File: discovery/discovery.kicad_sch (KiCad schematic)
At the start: 19 parts, among them J1 USB_C_Receptacle_USB2.0_16P, SW1 SW_Push, U1 RP2350_60QFN, U2 USBLC6-2SC6, U3 AP2114H-3.3TRG1, U4 W25Q32JVZP, X1 ABM8-272-T3

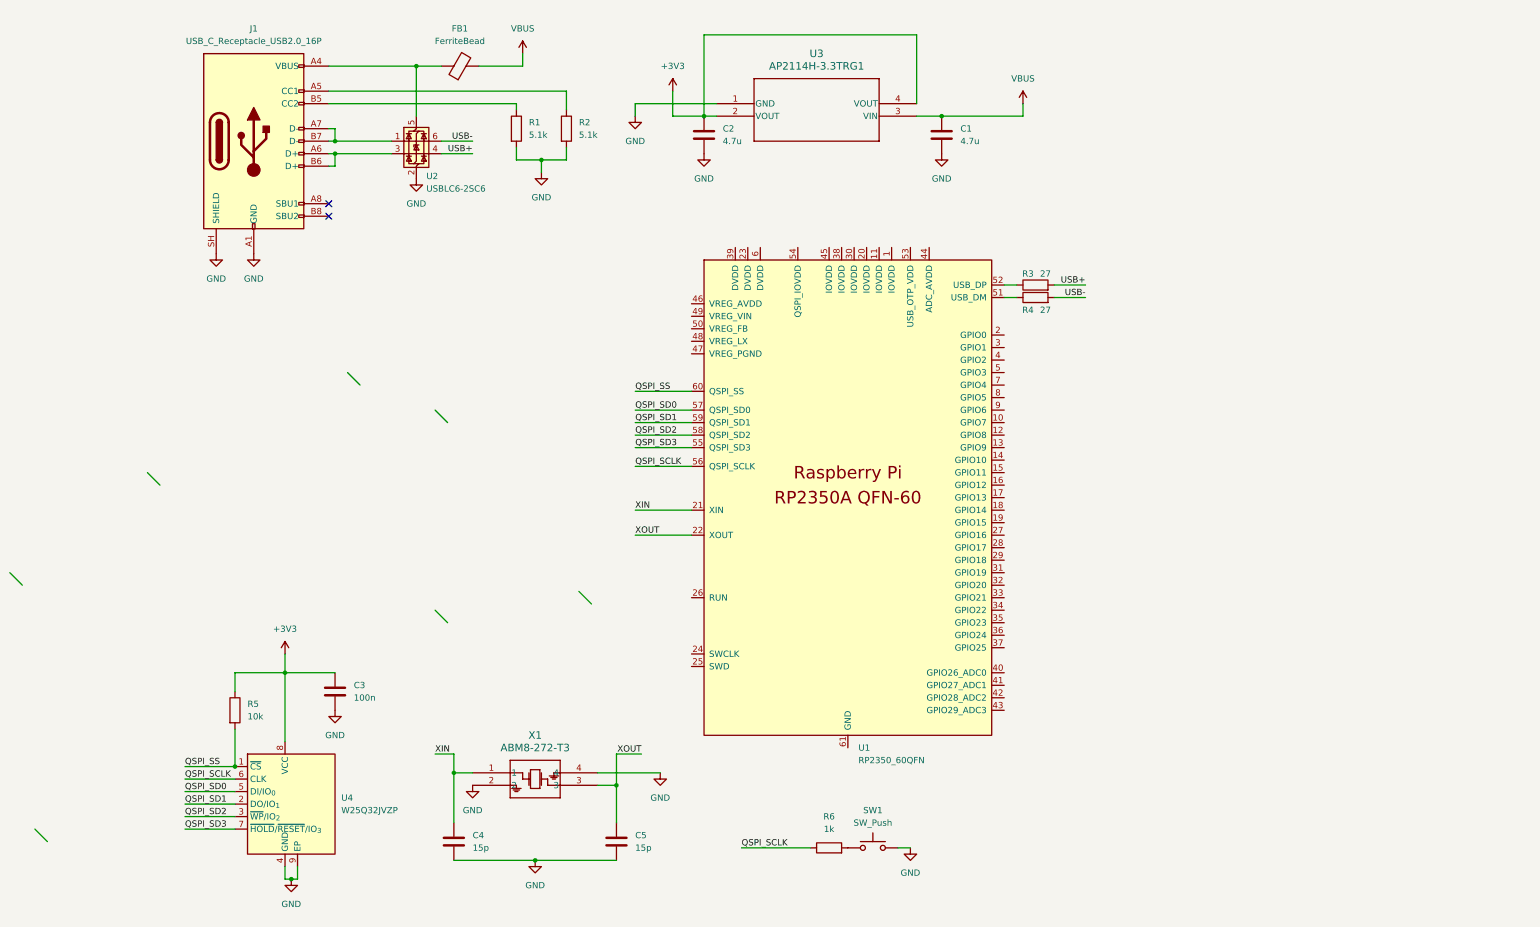
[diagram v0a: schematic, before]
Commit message: add inductor
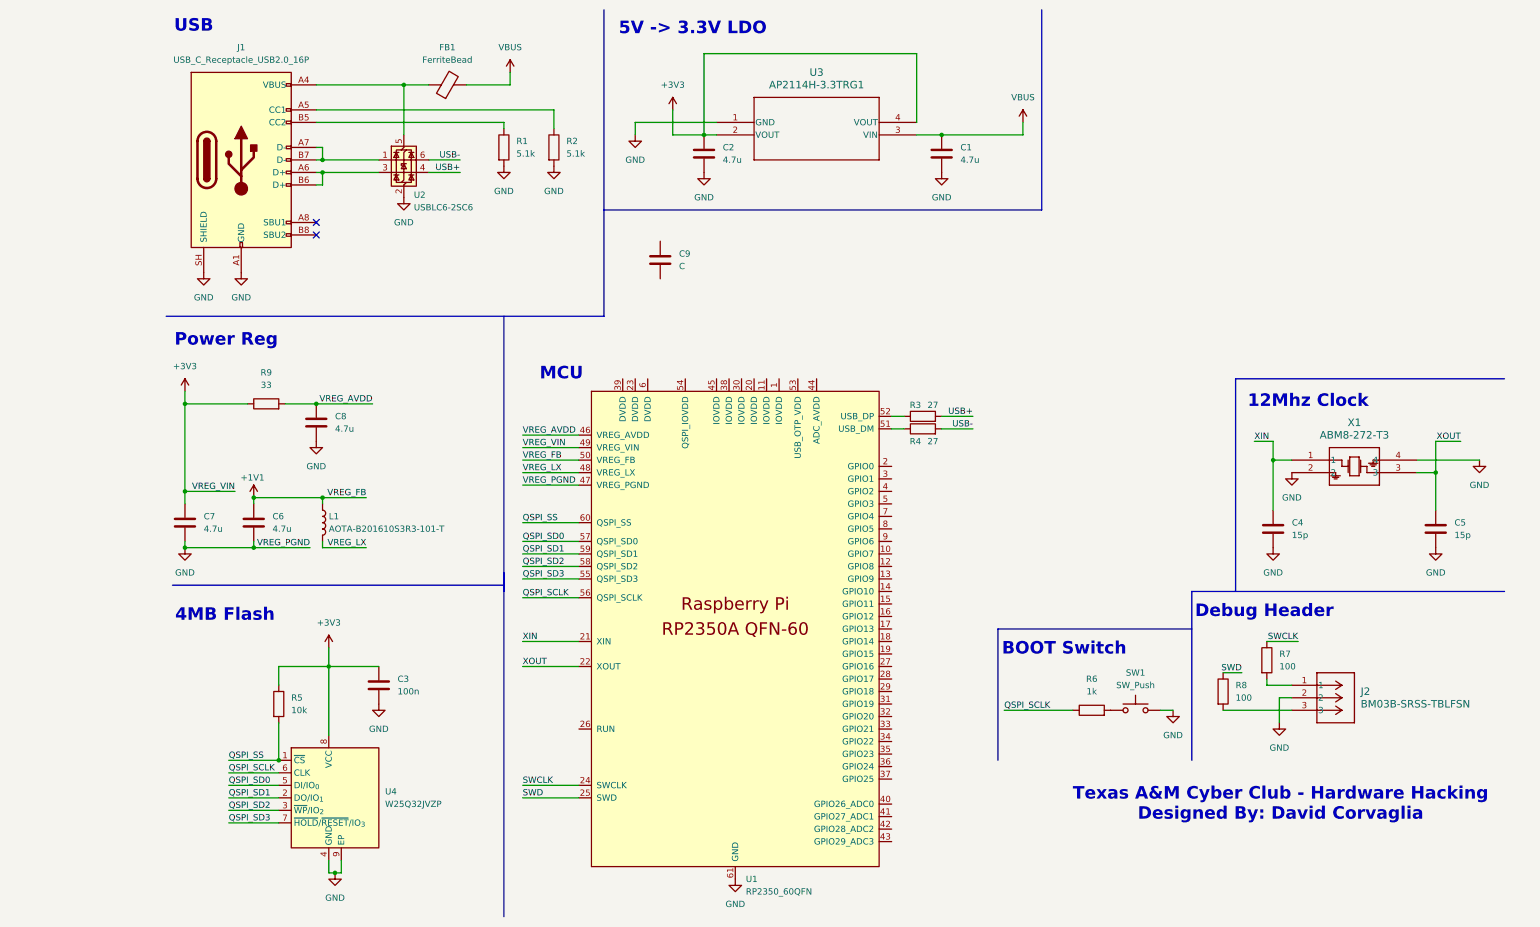
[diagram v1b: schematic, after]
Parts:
- added C6, C7, C8: 4.7u, symbol Device:C
- added C9: C, symbol Device:C
- added J2: BM03B-SRSS-TBLFSN, footprints:CONN_BM03B-SRSS-TBLFSN_JST, symbol lib:BM03B-SRSS-TBLFSN
- added L1: AOTA-B201610S3R3-101-T, footprints:L_pol_2016, symbol Device:L
- added R7, R8: 100, symbol Device:R
- added R9: 33, symbol Device:R
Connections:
- net +3V3: now also U1.49 (VREG_VIN), C7.1, R9.1
- net GND: now also U1.47 (VREG_PGND), U1.61 (GND), C6.2, C7.2, C8.2, J2.2
- net SWCLK: now reaches U1.24 (SWCLK)
- net SWCLK: now also R7.1
- net SWD: now reaches U1.25 (SWD)
- net SWD: now also R8.1
- net VREG_AVDD: now reaches U1.46 (VREG_AVDD)
- net VREG_AVDD: now also C8.1, R9.2
- net VREG_LX: now reaches U1.48 (VREG_LX)
- net VREG_LX: now also L1.2
- net +1V1: now reaches U1.50 (VREG_FB)
- net +1V1: now also C6.1, L1.1
- new net: J2.3, R8.2
- new net: J2.1, R7.2
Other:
- note added: "12Mhz Clock"
- note added: "4MB Flash"
- note added: "5V -> 3.3V LDO"
- note added: "BOOT Switch"
- note added: "Debug Header"
- note added: "MCU"
- note added: "Power Reg"
- note added: "Texas A&M Cyber Club - Hardware Hacking Designed By: David Corvaglia"
- note added: "USB"
- title: (none) -> Discovery PCB
- moved on the sheet: C1, C2, C3, C4, C5, FB1, J1, R1, R2, R3, R4, R5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

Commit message: make all components 0402 for the caps and resistors
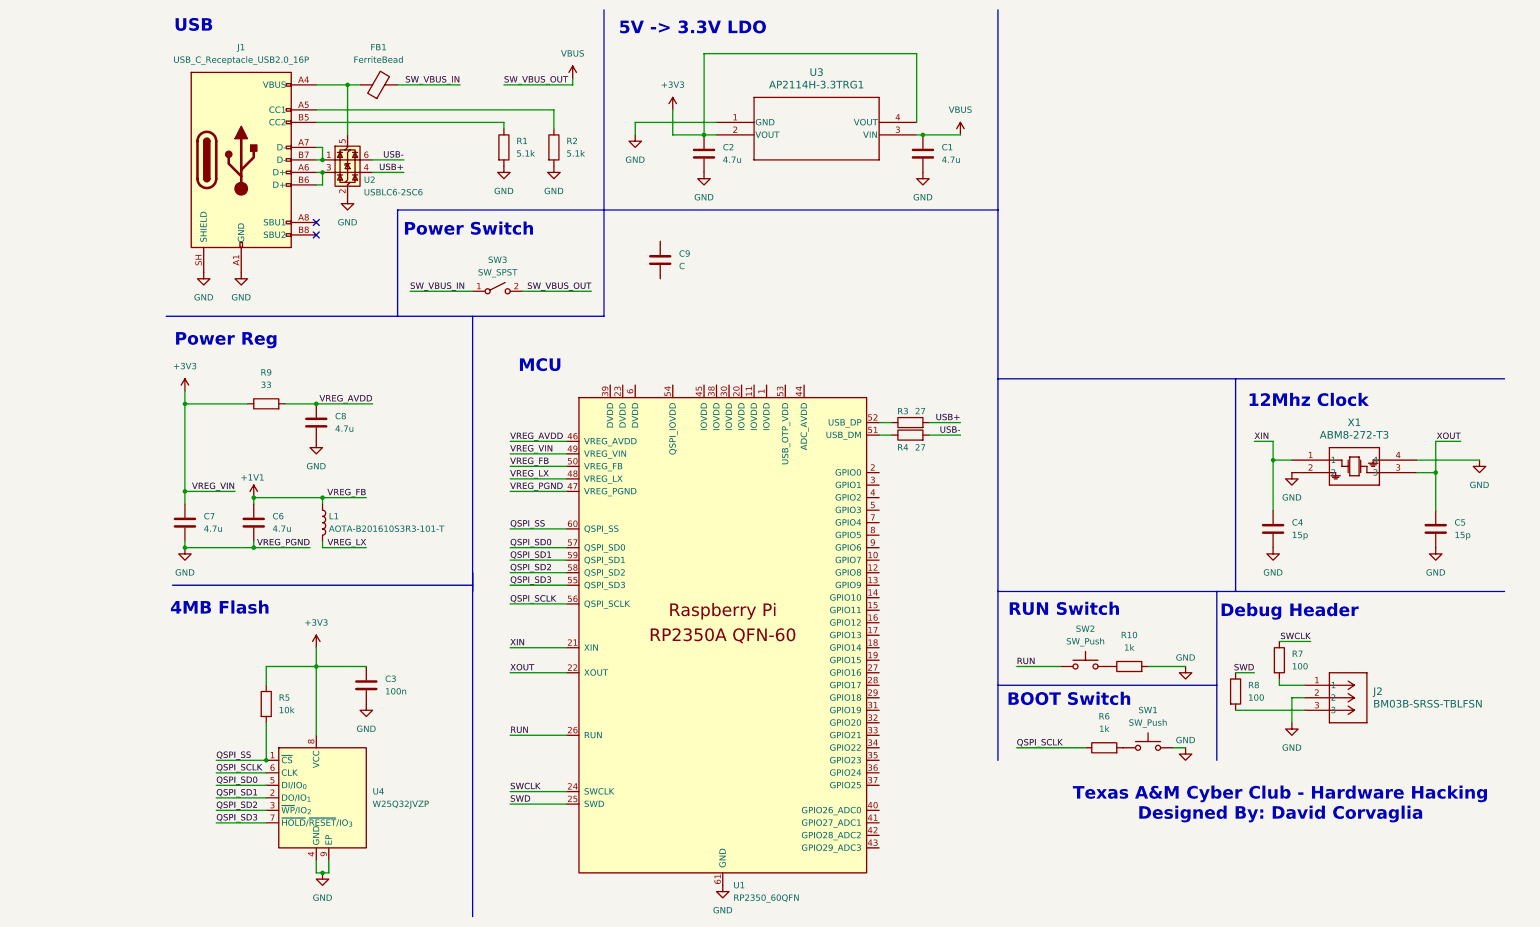
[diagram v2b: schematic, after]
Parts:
- added R10: 1k, Resistor_SMD:R_0402_1005Metric, symbol Device:R
- added SW2: SW_Push, symbol Switch:SW_Push
- added SW3: SW_SPST, symbol Switch:SW_SPST
- C1, C2, C3, C4, C5, C6, C7, C8: footprint (none) -> Capacitor_SMD:C_0402_1005Metric
- FB1: footprint (none) -> Inductor_SMD:L_0402_1005Metric
- R1, R2, R3, R4, R5, R6, R7, R8, R9: footprint (none) -> Resistor_SMD:R_0402_1005Metric
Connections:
- net GND: now also R10.2
- net VBUS: now also SW3.2 (B); no longer FB1.2
- net RUN: now reaches U1.26 (RUN)
- net RUN: now also SW2.1
- new net: R10.1, SW2.2
- new net SW_VBUS_IN: FB1.2, SW3.1 (A)
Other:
- note added: "Power Switch"
- note added: "RUN Switch"
- moved on the sheet: C1, C3, FB1, J2, R3, R4, R5, R6, R7, R8, SW1, U1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
